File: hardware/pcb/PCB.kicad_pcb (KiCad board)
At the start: 2 copper layers, 55 x 95 mm, 47 parts, among them J1 USB_A, J2 AudioJack3, J3 USB_B_Micro, Q1 BSS138, Q2 MMBT3904, Q3 MMBT3904, SW1 RESET, SW2 S4, SW3 BOOT, SW4 RESET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

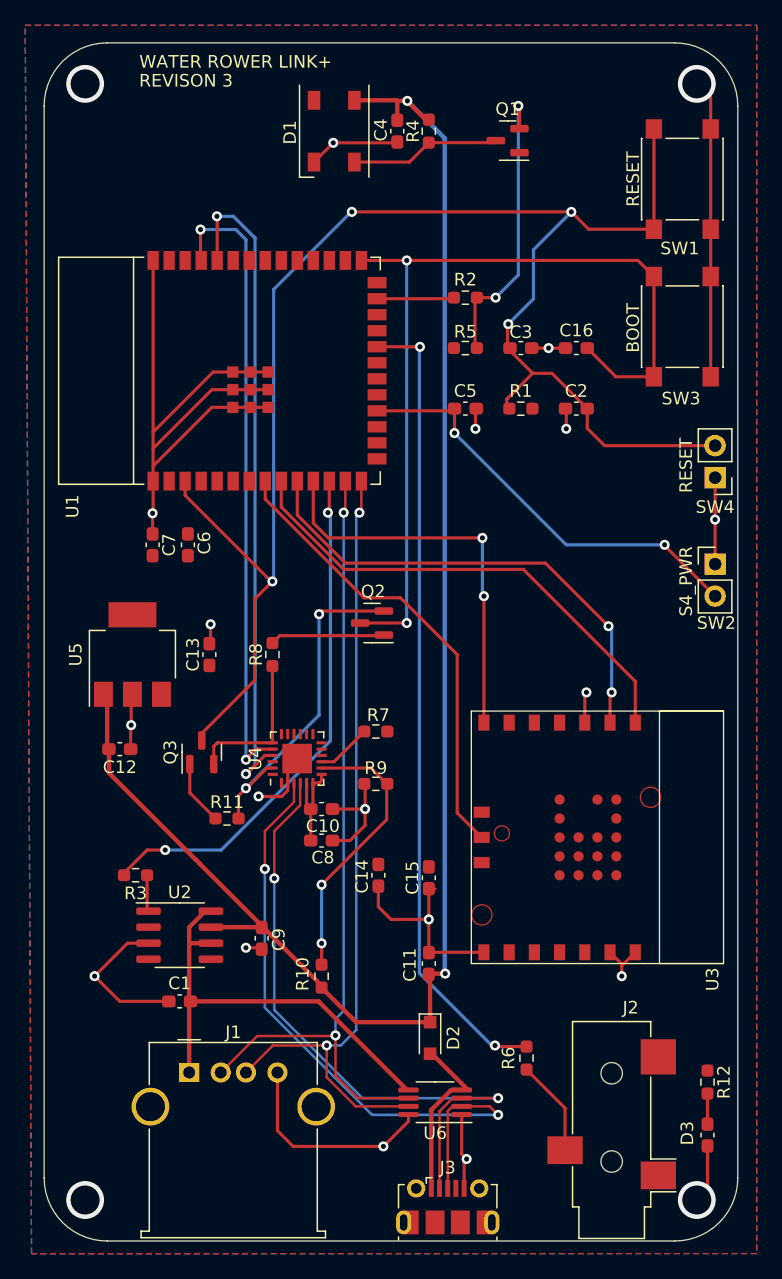
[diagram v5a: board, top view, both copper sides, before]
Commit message: Rev 3: increase screw hole size
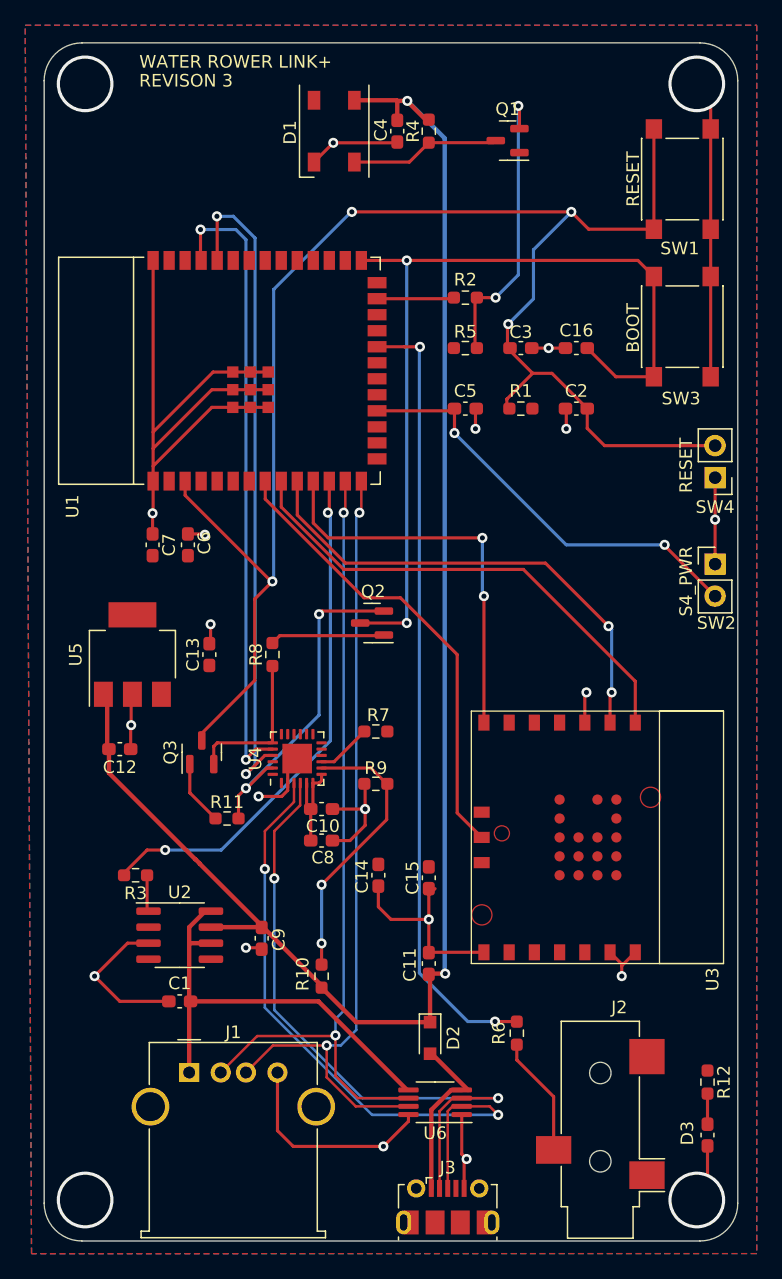
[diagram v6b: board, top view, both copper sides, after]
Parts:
- moved R6 2.12 mm to (136.5, 163.5)
- moved J2 0.90 mm to (143.1, 171.2)
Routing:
- net Net-(J2-PadR): track 7.65 -> 9.56 mm
- net Net-(R6-Pad2): track 64.0 -> 62.4 mm
- net Earth: track 179.6 -> 180.9 mm, vias 21 -> 22
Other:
- outline, holes or cut-outs redrawn
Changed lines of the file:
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@@
   )
   (footprint "Resistor_SMD:R_0603_1608Metric_Pad0.98x0.95mm_HandSolder" placed (layer "F.Cu")
-    (at 137.25 165.5 90)
+    (at 136.48 163.52 90)
     (descr "Resistor SMD 0603 (1608 Metric), square (rectangular) end terminal, IPC_7351 nominal with elongated pad for handsoldering. (Body size source: IPC-SM-782 page 72, https://www.pcb-3d.com/wordpress/wp-content/uploads/ipc-sm-782a_amendment_1_and_2.pdf), generated with kicad-footprint-generator")
     (tags "resistor handsolder")
@@
   )
   (footprint "Connector_Audio:Jack_3.5mm_CUI_SJ-3523-SMT_Horizontal" (layer "F.Cu")
-    (at 144 171.2 180)
+    (at 143.1 171.18 180)
     (descr "3.5 mm, Stereo, Right Angle, Surface Mount (SMT), Audio Jack Connector (https://www.cui.com/product/resource/sj-352x-smt-series.pdf)")
     (tags "3.5mm audio cui horizontal jack stereo")
@@
     )
   )
-  (gr_arc locked (start 149 85) (mid 152.535534 86.464466) (end 154 90) (layer "Edge.Cuts") (width 0.1))
-  (gr_line locked (start 154 90) (end 154 175) (layer "Edge.Cuts") (width 0.1))
-  (gr_arc locked (start 104 180) (mid 100.464466 178.535534) (end 99 175) (layer "Edge.Cuts") (width 0.1))
-  (gr_line locked (start 104 85) (end 149 85) (layer "Edge.Cuts") (width 0.1))
-  (gr_line locked (start 99 90) (end 99 175) (layer "Edge.Cuts") (width 0.1))
-  (gr_line locked (start 104 180) (end 149 180) (layer "Edge.Cuts") (width 0.1))
-  (gr_arc locked (start 154 175) (mid 152.535534 178.535534) (end 149 180) (layer "Edge.Cuts") (width 0.1))
-  (gr_arc locked (start 99 90) (mid 100.464466 86.464466) (end 104 85) (layer "Edge.Cuts") (width 0.1))
+  (gr_arc locked (start 151 85) (mid 153.12132 85.87868) (end 154 88) (layer "Edge.Cuts") (width 0.1))
+  (gr_line locked (start 154 88) (end 154 177) (layer "Edge.Cuts") (width 0.1))
+  (gr_arc locked (start 102 180) (mid 99.87868 179.12132) (end 99 177) (layer "Edge.Cuts") (width 0.1))
+  (gr_line locked (start 102 85) (end 151 85) (layer "Edge.Cuts") (width 0.1))
+  (gr_line locked (start 99 88) (end 99 177) (layer "Edge.Cuts") (width 0.1))
+  (gr_line locked (start 102 180) (end 151 180) (layer "Edge.Cuts") (width 0.1))
+  (gr_arc locked (start 154 177) (mid 153.12132 179.12132) (end 151 180) (layer "Edge.Cuts") (width 0.1))
+  (gr_arc locked (start 99 88) (mid 99.87868 85.87868) (end 102 85) (layer "Edge.Cuts") (width 0.1))
   (gr_text "REVISON 3" (at 110.25 88) (layer "F.SilkS")
     (effects (font (size 1 1) (thickness 0.15)))
@@
   (segment (start 105.9 139.1) (end 105.9 136.75) (width 0.25) (layer "F.Cu") (net 6))
   (segment (start 132.1125 169.975) (end 132.1125 173.1125) (width 0.25) (layer "F.Cu") (net 6))
+  (segment (start 111.6875 123.9375) (end 111.75 124) (width 0.25) (layer "F.Cu") (net 6))
   (segment (start 132.3 173.7) (end 132.3 175.8295) (width 0.25) (layer "F.Cu") (net 6))
   (segment (start 152.2 122.8) (end 152.2 126.325) (width 0.25) (layer "F.Cu") (net 6))
@@
   (segment (start 129.5 157.1375) (end 129.5 154.5) (width 0.25) (layer "F.Cu") (net 6))
   (segment (start 144.8 158.180501) (end 145.8715 157.109001) (width 0.25) (layer "F.Cu") (net 6))
+  (segment (start 110.4 123.9375) (end 111.6875 123.9375) (width 0.25) (layer "F.Cu") (net 6))
   (segment (start 124.4495 147.0505) (end 123.25 148.25) (width 0.25) (layer "F.Cu") (net 6))
   (segment (start 139 109.2) (end 137.6625 109.2) (width 0.25) (layer "F.Cu") (net 6))
@@
   (via (at 139 109.2) (size 0.8) (drill 0.4) (layers "F.Cu" "B.Cu") (free) (net 6))
   (via (at 125.9 172.5) (size 0.8) (drill 0.4) (layers "F.Cu" "B.Cu") (net 6))
-  (via locked (at 150.75 176.75) (size 3) (drill 2.3) (layers "F.Cu" "B.Cu") (free) (net 6))
+  (via locked (at 150.75 176.75) (size 4.5) (drill 4) (layers "F.Cu" "B.Cu") (free) (net 6))
   (via (at 121.925 92.925) (size 0.8) (drill 0.4) (layers "F.Cu" "B.Cu") (net 6))
   (via (at 115 156.75) (size 0.8) (drill 0.4) (layers "F.Cu" "B.Cu") (free) (net 6))
@@
   (via (at 140.4 115.6) (size 0.8) (drill 0.4) (layers "F.Cu" "B.Cu") (free) (net 6))
   (via (at 124.4495 145.75) (size 0.8) (drill 0.4) (layers "F.Cu" "B.Cu") (free) (net 6))
-  (via locked (at 102.25 176.75) (size 3) (drill 2.3) (layers "F.Cu" "B.Cu") (free) (net 6))
+  (via locked (at 102.25 176.75) (size 4.5) (drill 4) (layers "F.Cu" "B.Cu") (free) (net 6))
   (via (at 103 159) (size 0.8) (drill 0.4) (layers "F.Cu" "B.Cu") (net 6))
   (via (at 144.8 159) (size 0.8) (drill 0.4) (layers "F.Cu" "B.Cu") (free) (net 6))
@@
   (via (at 107.6 122.3) (size 0.8) (drill 0.4) (layers "F.Cu" "B.Cu") (free) (net 6))
   (via (at 105.9 139.1) (size 0.8) (drill 0.4) (layers "F.Cu" "B.Cu") (free) (net 6))
-  (via locked (at 150.75 88.25) (size 3) (drill 2.3) (layers "F.Cu" "B.Cu") (free) (net 6))
-  (via locked (at 102.25 88.25) (size 3) (drill 2.3) (layers "F.Cu" "B.Cu") (free) (net 6))
+  (via (at 111.75 124) (size 0.8) (drill 0.4) (layers "F.Cu" "B.Cu") (free) (net 6))
+  (via locked (at 150.75 88.25) (size 4.5) (drill 4) (layers "F.Cu" "B.Cu") (free) (net 6))
+  (via locked (at 102.25 88.25) (size 4.5) (drill 4) (layers "F.Cu" "B.Cu") (free) (net 6))
   (segment (start 121 142) (end 121.9875 142) (width 0.25) (layer "F.Cu") (net 7))
   (segment (start 121.9875 142) (end 124.3875 139.6) (width 0.25) (layer "F.Cu") (net 7))
-  (segment (start 140.3 172.8) (end 140.3 169.4625) (width 0.25) (layer "F.Cu") (net 8))
-  (segment (start 140.3 169.4625) (end 137.25 166.4125) (width 0.25) (layer "F.Cu") (net 8))
+  (segment (start 136.48 164.4325) (end 136.48 165.6425) (width 0.25) (layer "F.Cu") (net 8))
+  (segment (start 136.48 165.6425) (end 139.4 168.5625) (width 0.25) (layer "F.Cu") (net 8))
+  (segment (start 139.4 172.78) (end 139.4 168.5625) (width 0.25) (layer "F.Cu") (net 8))
   (segment (start 107.1625 151) (end 107.1625 153.7325) (width 0.25) (layer "F.Cu") (net 9))
   (segment (start 127.75 131) (end 124.0625 131) (width 0.25) (layer "F.Cu") (net 10))
@@
   (segment (start 113.037114 149) (end 121.7 140.337114) (width 0.25) (layer "B.Cu") (net 54))
   (segment (start 121.7 140.337114) (end 121.7 122.45) (width 0.25) (layer "B.Cu") (net 54))
-  (segment (start 134.8375 164.5875) (end 137.25 164.5875) (width 0.25) (layer "F.Cu") (net 55))
   (segment (start 127.6 109.1) (end 127.595 109.095) (width 0.25) (layer "F.Cu") (net 55))
   (segment (start 127.595 109.095) (end 125.4 109.095) (width 0.25) (layer "F.Cu") (net 55))
-  (segment (start 134.75 164.5) (end 134.8375 164.5875) (width 0.25) (layer "F.Cu") (net 55))
+  (segment (start 134.75 162.6) (end 136.4725 162.6) (width 0.25) (layer "F.Cu") (net 55))
   (segment (start 128.8 109.1) (end 127.6 109.1) (width 0.25) (layer "F.Cu") (net 55))
   (via (at 128.8 109.1) (size 0.8) (drill 0.4) (layers "F.Cu" "B.Cu") (net 55))
-  (via (at 134.75 164.5) (size 0.8) (drill 0.4) (layers "F.Cu" "B.Cu") (net 55))
-  (segment (start 128.75 158.75) (end 134.5 164.5) (width 0.25) (layer "B.Cu") (net 55))
-  (segment (start 134.5 164.5) (end 134.75 164.5) (width 0.25) (layer "B.Cu") (net 55))
-  (segment (start 128.75 109.15) (end 128.75 158.75) (width 0.25) (layer "B.Cu") (net 55))
-  (segment (start 128.8 109.1) (end 128.75 109.15) (width 0.25) (layer "B.Cu") (net 55))
+  (via (at 134.75 162.6) (size 0.8) (drill 0.4) (layers "F.Cu" "B.Cu") (net 55))
+  (segment (start 128.75 158.75) (end 128.75 109.15) (width 0.25) (layer "B.Cu") (net 55))
+  (segment (start 128.75 109.15) (end 128.8 109.1) (width 0.25) (layer "B.Cu") (net 55))
+  (segment (start 132.6 162.6) (end 128.75 158.75) (width 0.25) (layer "B.Cu") (net 55))
+  (segment (start 134.75 162.6) (end 132.6 162.6) (width 0.25) (layer "B.Cu") (net 55))
   (segment (start 127.9625 94.45) (end 129.5 92.9125) (width 0.25) (layer "F.Cu") (net 95))
   (segment (start 129.5 92.9125) (end 134.65 92.9125) (width 0.25) (layer "F.Cu") (net 95))

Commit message: R4 screw hole clearance
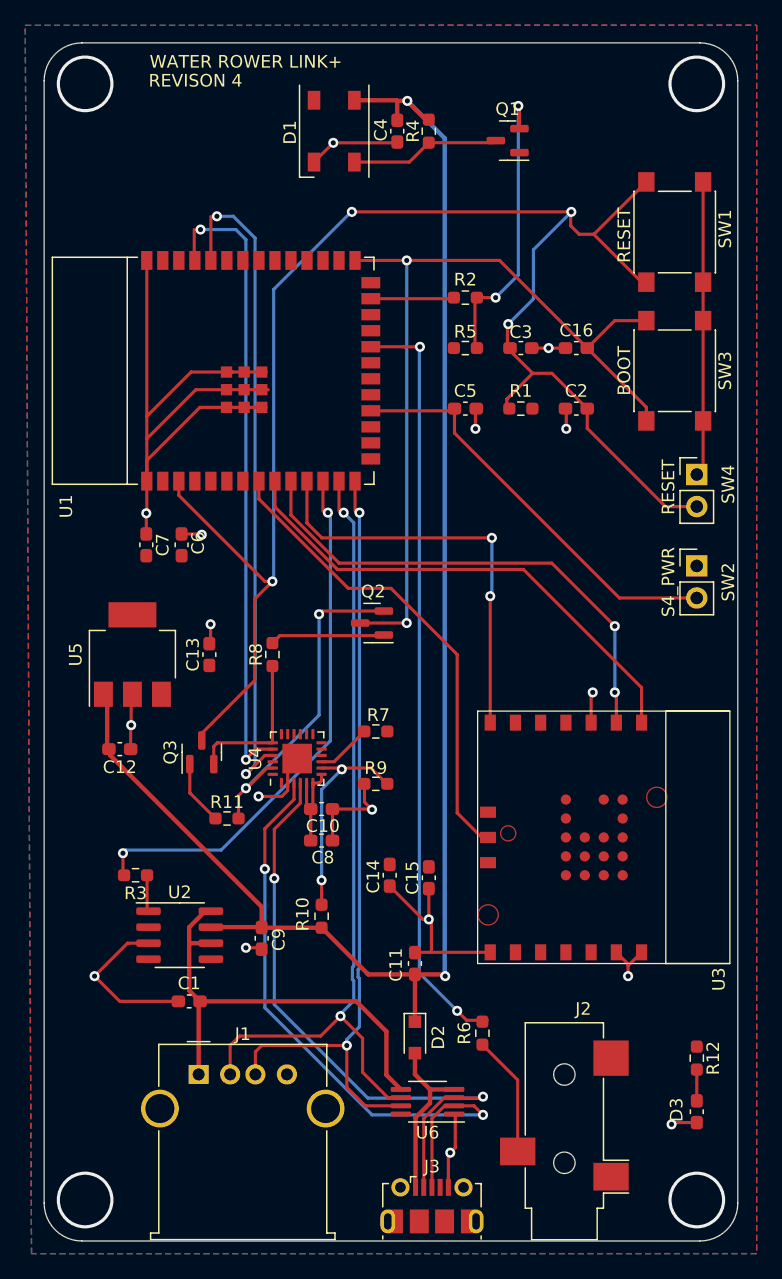
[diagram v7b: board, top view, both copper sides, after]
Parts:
- moved R10 4.75 mm to (121.0, 154.2)
- moved SW1 4.24 mm to (149.0, 100.0)
- moved SW3 3.55 mm to (149.0, 111.0)
- moved J2 2.85 mm to (140.2, 171.3)
- moved R6 2.73 mm to (133.8, 163.5)
- moved R12 2.08 mm to (150.8, 165.5)
- moved D3 2.04 mm to (150.8, 169.8)
- moved SW4 1.47 mm to (150.8, 119.2), turned to 0 degrees
- moved SW2 1.46 mm to (150.8, 126.5)
- moved J3 1.25 mm to (129.8, 177.2)
- moved D2 1.20 mm to (128.4, 163.9)
- moved C11 1.10 mm to (128.4, 158.0)
- moved C14 0.90 mm to (126.4, 151.0)
- moved J1 0.76 mm to (111.2, 166.8)
- moved C1 0.75 mm to (110.5, 161.0)
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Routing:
- net Earth: track 180.9 -> 154.1 mm, vias 22 -> 21
- net Net-(R10-Pad2): track 22.2 -> 17.3 mm
- net BOOT: track 70.3 -> 66.5 mm
- net Net-(R6-Pad2): track 62.4 -> 60.0 mm
- net ESD_S4_DP: track 64.3 -> 62.6 mm
- net ESD_DN: track 50.7 -> 49.0 mm
- net S4_VBUS: track 35.0 -> 36.4 mm
- net ESD_DP: track 51.3 -> 49.9 mm
- net Net-(C5-Pad1): track 34.0 -> 32.5 mm, vias 2 -> 0
- net VBUS: track 126.8 -> 125.4 mm
- net ANT_RTS: track 31.9 -> 33.2 mm
- net CHIP_PU: track 126.3 -> 127.1 mm
- net ANT_TX: track 39.1 -> 39.8 mm
- net Net-(R3-Pad2): track 41.7 -> 42.4 mm
- net ESD_S4_DN: track 64.8 -> 64.2 mm
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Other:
- board text added: "REVISON 4"
- board text removed: "REVISON 3"

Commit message: Earth to GND
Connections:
- net Earth renamed GND
